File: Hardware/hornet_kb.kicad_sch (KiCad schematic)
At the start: 35 parts, among them J1 Conn_ST_STDC14, J10 USB_C_Receptacle_USB2.0, SW98 SW_Push, U1 nRF52840, Y1 32.768kHz, Y2 32MHz

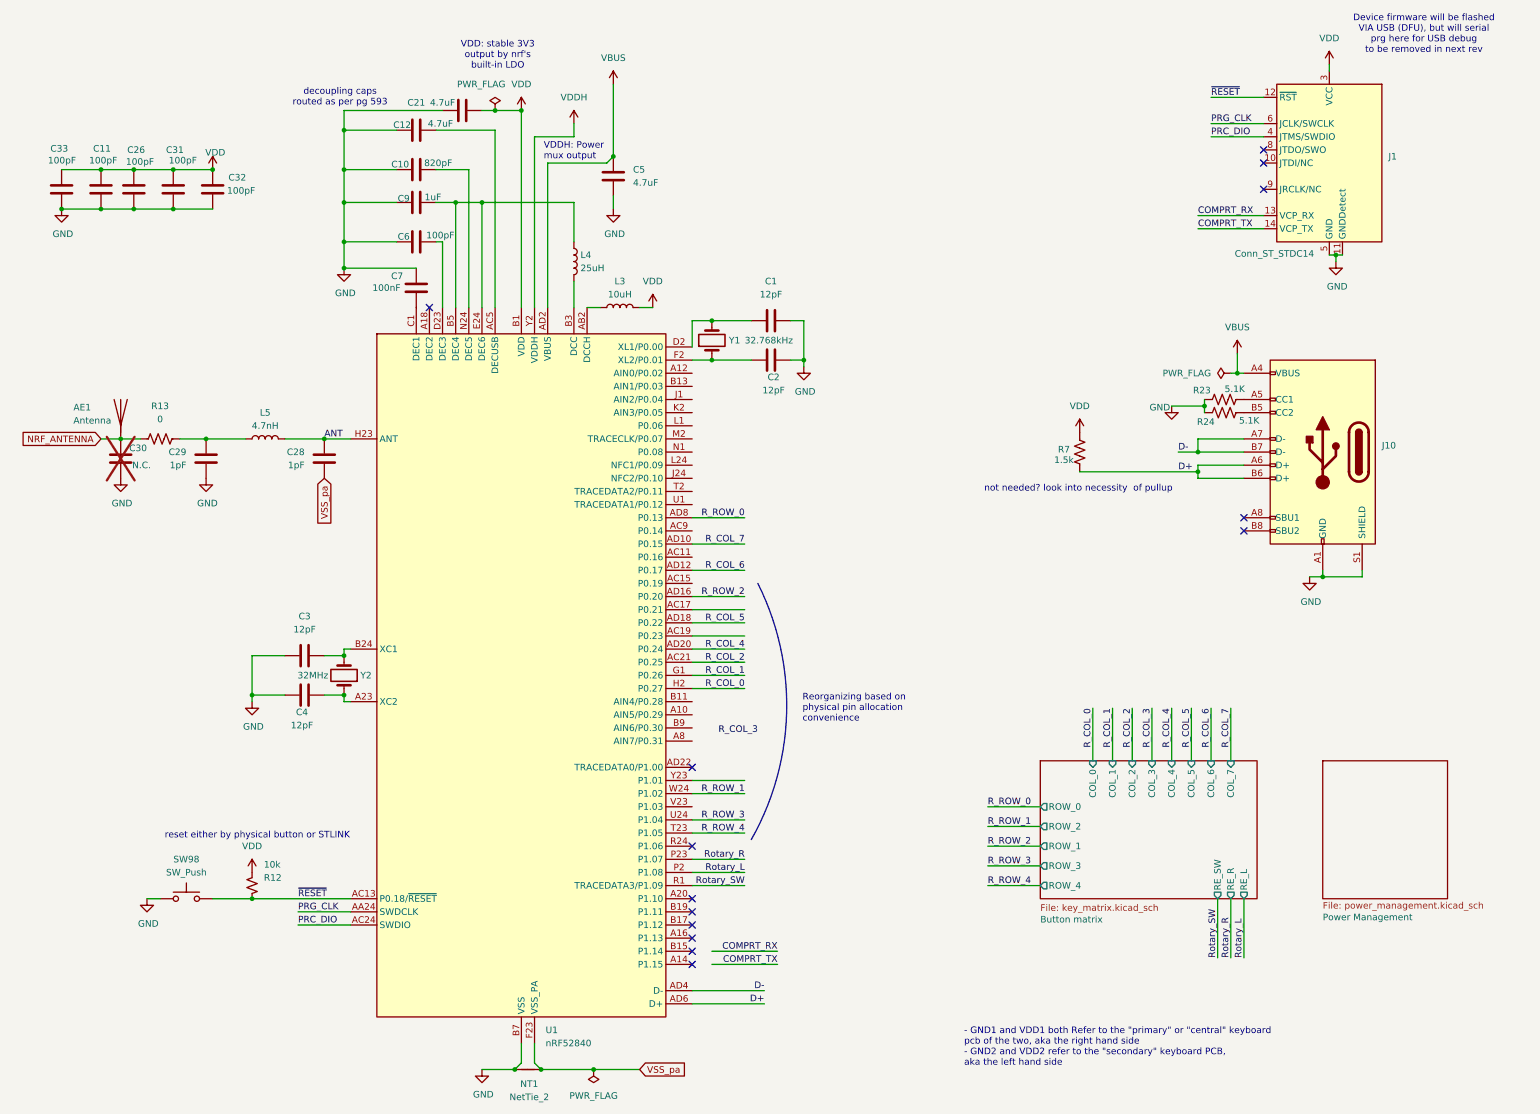
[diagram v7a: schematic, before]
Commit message: Fix ERC and stylistic errors
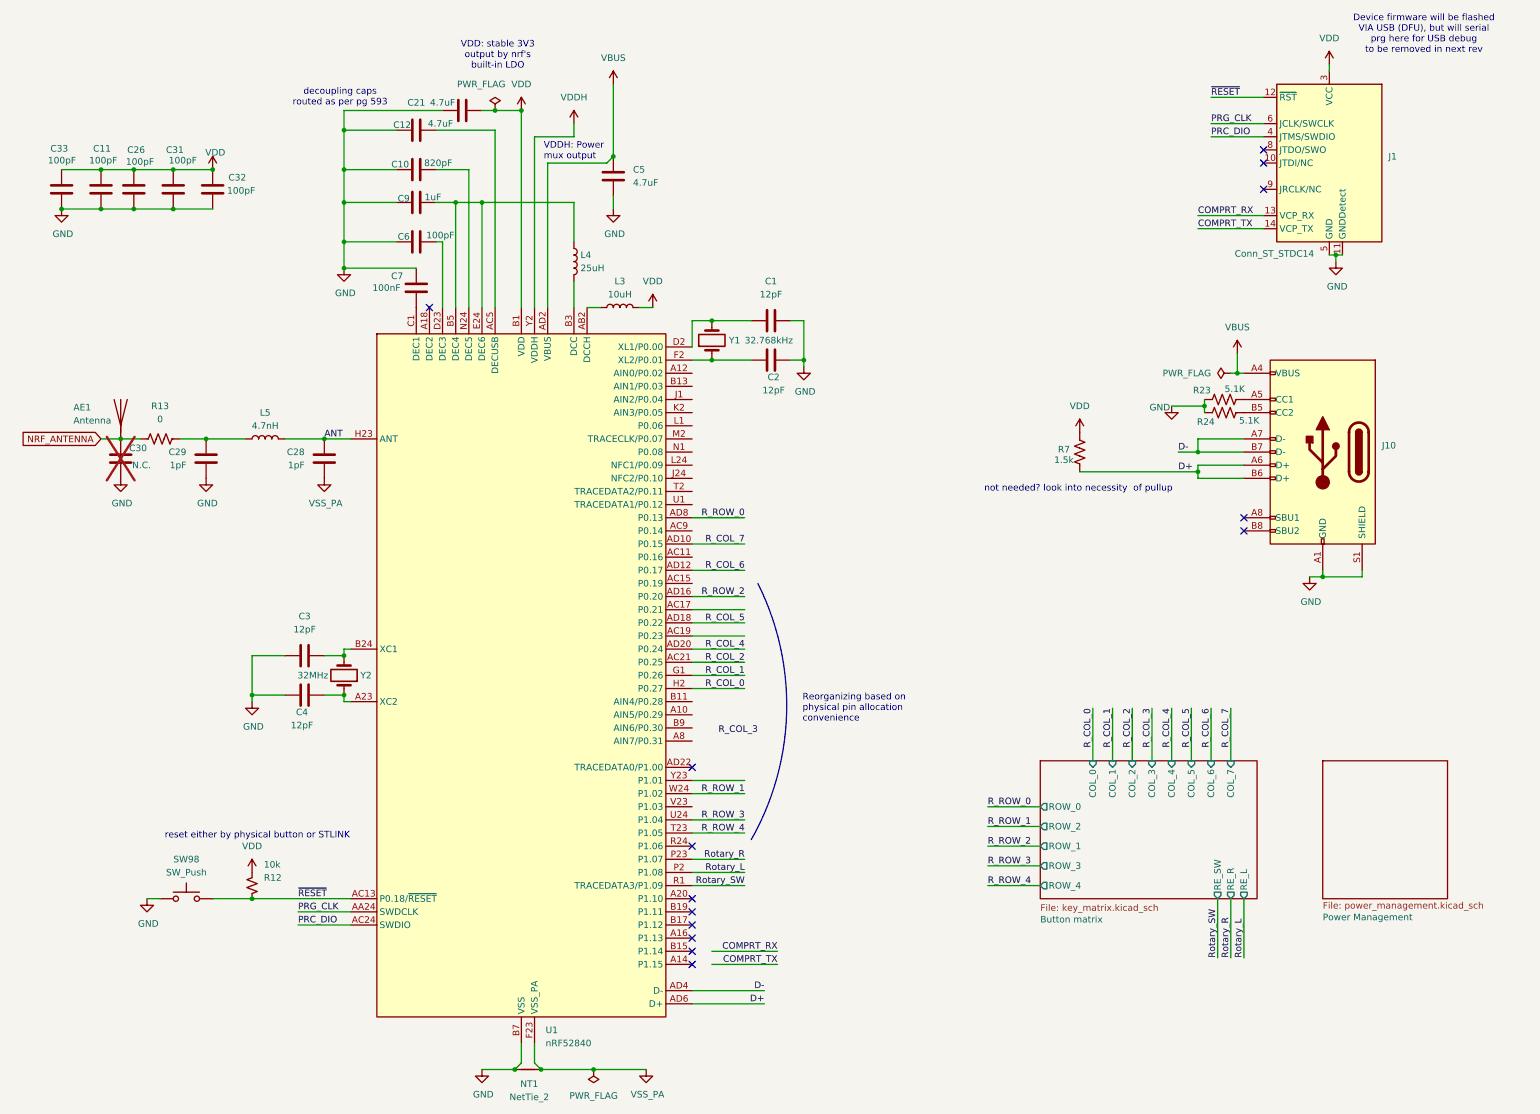
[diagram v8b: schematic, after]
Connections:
- net VSS_pa renamed VSS_PA
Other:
- note removed: "- GND1 and VDD1 both Refer to the "primary" or "central" keyboard pcb of the two, aka the right hand side - GND2 and VDD2 refer to the "secondary" keyboard PCB, aka the left hand side"
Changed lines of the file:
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@@
 		)
 	)
-	(text "- GND1 and VDD1 both Refer to the \"primary\" or \"central\" keyboard \npcb of the two, aka the right hand side\n- GND2 and VDD2 refer to the \"secondary\" keyboard PCB,\naka the left hand side"
-		(exclude_from_sim no)
-		(at 202.438 214.122 0)
-		(effects
-			(font
-				(size 1.27 1.27)
-			)
-			(justify left)
-		)
-	)
 	(text "Reorganizing based on \nphysical pin allocation \nconvenience"
 		(exclude_from_sim no)
@@
 	(wire
 		(pts
-			(xy 139.7 218.44) (xy 130.81 218.44)
+			(xy 140.97 218.44) (xy 130.81 218.44)
 		)
 		(stroke
@@
 		)
 	)
-	(global_label "VSS_pa"
-		(shape input)
-		(at 139.7 218.44 0)
-		(fields_autoplaced yes)
-		(effects
-			(font
-				(size 1.27 1.27)
-			)
-			(justify left)
-		)
-		(property "Intersheetrefs" "${INTERSHEET_REFS}"
-			(at 149.4584 218.44 0)
-			(effects
-				(font
-					(size 1.27 1.27)
-				)
-				(justify left)
-				(hide yes)
-			)
-		)
-	)
 	(global_label "NRF_ANTENNA"
 		(shape input)
@@
 		)
 	)
-	(global_label "VSS_pa"
-		(shape input)
-		(at 78.74 104.14 270)
-		(fields_autoplaced yes)
-		(effects
-			(font
-				(size 1.27 1.27)
-			)
-			(justify right)
-		)
-		(property "Intersheetrefs" "${INTERSHEET_REFS}"
-			(at 78.74 113.8984 90)
-			(effects
-				(font
-					(size 1.27 1.27)
-				)
-				(justify right)
-				(hide yes)
-			)
-		)
-	)
 	(symbol
 		(lib_id "Switch:SW_Push")
@@
 	)
 	(symbol
+		(lib_id "power:GND")
+		(at 78.74 104.14 0)
+		(mirror y)
+		(unit 1)
+		(exclude_from_sim no)
+		(in_bom yes)
+		(on_board yes)
+		(dnp no)
+		(property "Reference" "#PWR046"
+			(at 78.74 110.49 0)
+			(effects
+				(font
+					(size 1.27 1.27)
+				)
+				(hide yes)
+			)
+		)
+		(property "Value" "VSS_PA"
+			(at 78.994 108.966 0)
+			(effects
+				(font
+					(size 1.27 1.27)
+				)
+			)
+		)
+		(property "Footprint" ""
+			(at 78.74 104.14 0)
+			(effects
+				(font
+					(size 1.27 1.27)
+				)
+				(hide yes)
+			)
+		)
+		(property "Datasheet" ""
+			(at 78.74 104.14 0)
+			(effects
+				(font
+					(size 1.27 1.27)
+				)
+				(hide yes)
+			)
+		)
+		(property "Description" "Power symbol creates a global label with name \"GND\" , ground"
+			(at 78.74 104.14 0)
+			(effects
+				(font
+					(size 1.27 1.27)
+				)
+				(hide yes)
+			)
+		)
+		(pin "1"
+		)
+		(instances
+			(project "hornet_kb"
+				(path "/c35084ab-104c-4a4c-9388-a839989b8e3d"
+					(reference "#PWR046")
+					(unit 1)
+				)
+			)
+		)
+	)
+	(symbol
 		(lib_id "Device:C")
 		(at 78.74 100.33 0)
@@
 					(unit 1)
 				)
+			)
+		)
+	)
+	(symbol
+		(lib_id "power:GND")
+		(at 140.97 218.44 0)
+		(mirror y)
+		(unit 1)
+		(exclude_from_sim no)
+		(in_bom yes)
+		(on_board yes)
+		(dnp no)
+		(property "Reference" "#PWR045"
+			(at 140.97 224.79 0)
+			(effects
+				(font
+					(size 1.27 1.27)
+				)
+				(hide yes)
+			)
+		)
+		(property "Value" "VSS_PA"
+			(at 141.224 223.266 0)
+			(effects
+				(font
+					(size 1.27 1.27)
+				)
+			)
+		)
+		(property "Footprint" ""
+			(at 140.97 218.44 0)
+			(effects
+				(font
+					(size 1.27 1.27)
+				)
+				(hide yes)
+			)
+		)
+		(property "Datasheet" ""
+			(at 140.97 218.44 0)
+			(effects
+				(font
+					(size 1.27 1.27)
+				)
+				(hide yes)
+			)
+		)
+		(property "Description" "Power symbol creates a global label with name \"GND\" , ground"
+			(at 140.97 218.44 0)
+			(effects
+				(font
+					(size 1.27 1.27)
+				)
+				(hide yes)
+			)
+		)
+		(pin "1"
+		)
+		(instances
+			(project "hornet_kb"
+				(path "/c35084ab-104c-4a4c-9388-a839989b8e3d"
+					(reference "#PWR045")
+					(unit 1)
+				)
